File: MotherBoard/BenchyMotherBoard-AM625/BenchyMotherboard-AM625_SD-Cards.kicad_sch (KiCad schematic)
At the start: 60 parts, among them J11 472192001, J12 MEM2075-00-140-01-A, U1 AM6254ATCGGAALW, U22 EMMC256-TY29-5B101, U27 IP4252CZ16-8-TTL, U28 IP4252CZ16-8-TTL, U29 SIP32510DT-T1-GE3, U30 SIP32510DT-T1-GE3, U32 74LVC1G08GW,125, U43 74LVC1G08GW,125, U44 74LVC1G08GW,125, U45 74LVC1G08GW,125

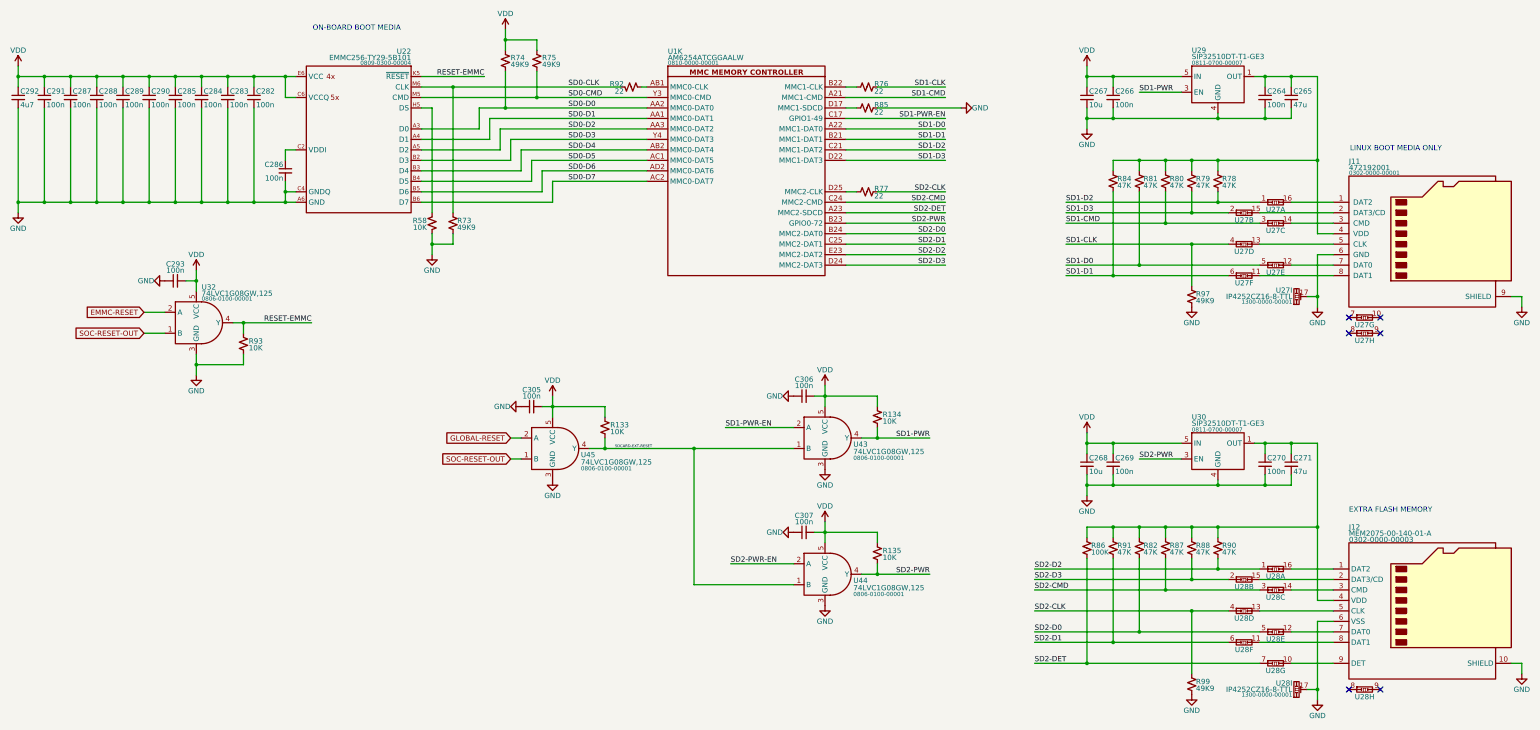
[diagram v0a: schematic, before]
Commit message: Schematic capture mostly complete. Starting PCB layout
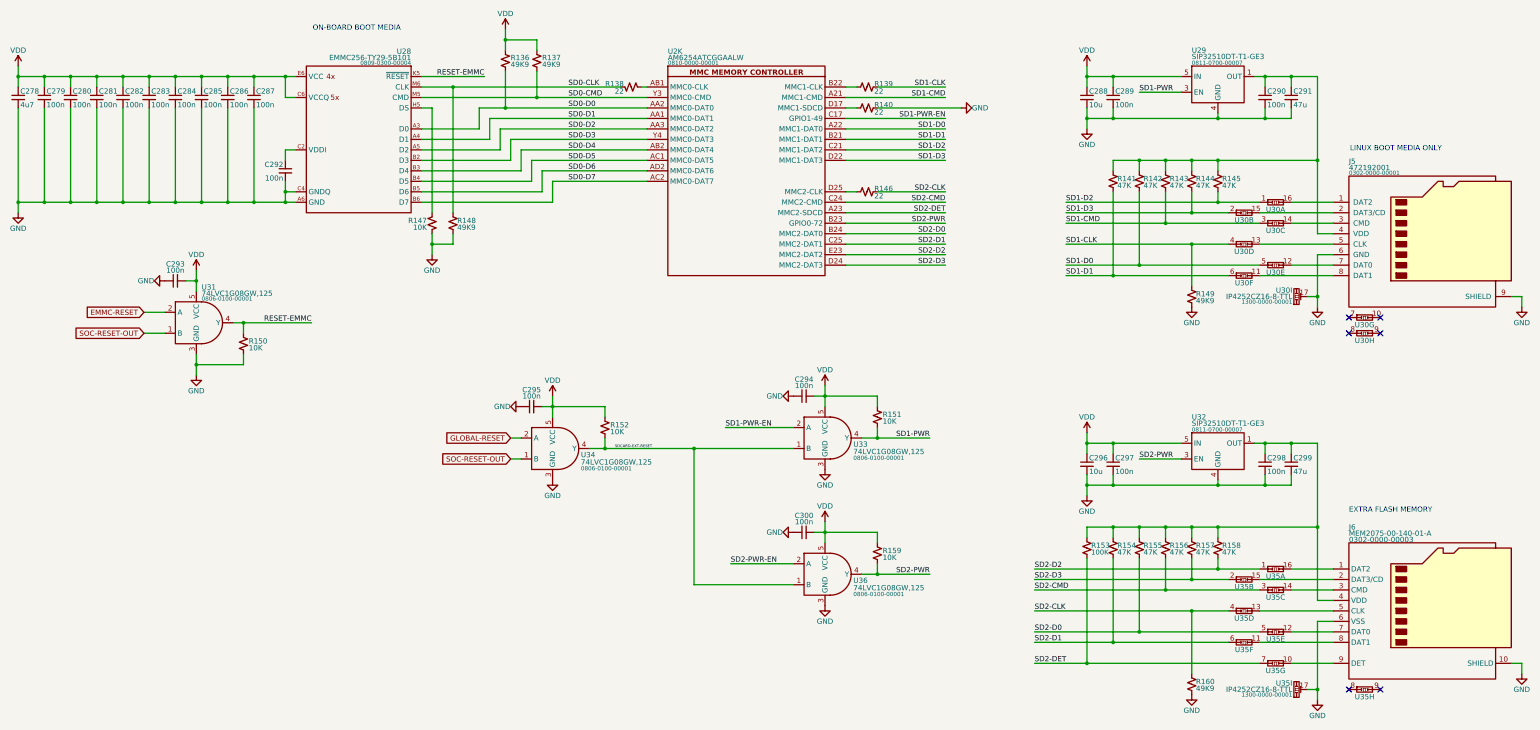
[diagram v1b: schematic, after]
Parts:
- renumbered C292 to C278, C291 to C279, C287 to C280, C288 to C281, C289 to C282, C290 to C283, C285 to C284, C284 to C285, C283 to C286, C282 to C287, C267 to C288, C266 to C289, C264 to C290, C265 to C291, C286 to C292, C306 to C294, C305 to C295, C268 to C296, C269 to C297, C270 to C298, C271 to C299, C307 to C300, J11 to J5, J12 to J6, R74 to R136, R75 to R137, R92 to R138, R76 to R139, R85 to R140, R84 to R141, R81 to R142, R80 to R143, R79 to R144, R78 to R145, R77 to R146, R58 to R147, R73 to R148, R97 to R149, R93 to R150, R134 to R151, R133 to R152, R86 to R153, R91 to R154, R82 to R155, R87 to R156, R88 to R157, R90 to R158, R135 to R159, R99 to R160, U1 to U2, U22 to U28, U27 to U30, U32 to U31, U30 to U32, U43 to U33, U45 to U34, U28 to U35, U44 to U36
